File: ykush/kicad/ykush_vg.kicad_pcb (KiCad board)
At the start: 2 copper layers, 89.9 x 54.9 mm, 61 parts, among them J1 USB-C 16P, J2 USB-A port, J3 USB-A port, J4 USB-A port, J5 EXT 5V, SW1 BOOT, U1 FE1.1s, U2 USBLC6-2SC6, U3 CH552G, U4 SY6280AAC, U5 USBLC6-2SC6, U6 SY6280AAC, U7 USBLC6-2SC6, U8 SY6280AAC, U9 USBLC6-2SC6, Y1 12MHz

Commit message: YKUSH-VG: rework USB-C entry (JP1 on D-, VBUS via B.Cu spine, drop upstream ESD), move hub decoupling
Board file is still work in progress (routing run in progress).

Co-Authored-By: Claude Opus 5.5 <noreply@anthropic.com>
Claude-Session: https://claude.ai/code/session_01EEWbo5vCC8AQXSYmE1aT85
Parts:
- removed U9: USBLC6-2SC6, Package_TO_SOT_SMD:SOT-23-6
- U2: value USBLC6-2SC6 -> CH552G; footprint Package_TO_SOT_SMD:SOT-23-6 -> Package_SO:SOIC-16_3.9x9.9mm_P1.27mm
- U3: value CH552G -> SY6280AAC; footprint Package_SO:SOIC-16_3.9x9.9mm_P1.27mm -> Package_TO_SOT_SMD:SOT-23-5
- U4, U6, U8: value SY6280AAC -> USBLC6-2SC6; footprint Package_TO_SOT_SMD:SOT-23-5 -> Package_TO_SOT_SMD:SOT-23-6
- U5, U7: value USBLC6-2SC6 -> SY6280AAC; footprint Package_TO_SOT_SMD:SOT-23-6 -> Package_TO_SOT_SMD:SOT-23-5
- moved U7 32.9 mm to (181.4, 93.3), turned to 0 degrees
- moved U3 28.1 mm to (115.8, 93.3), turned to 180 degrees
- moved U5 24.5 mm to (144.4, 94.1), turned to 180 degrees
- moved U2 16.7 mm to (139.2, 77.7)
- moved C6 16.0 mm to (154.7, 88.7), turned to -90 degrees
- moved C5 13.7 mm to (156.6, 88.7), turned to -90 degrees
- moved U4 6.37 mm to (120.2, 97.9), turned to 90 degrees
- moved U8 6.37 mm to (177.0, 97.9), turned to 90 degrees
- moved U6 5.81 mm to (148.8, 97.9), turned to 90 degrees
- moved C3 5.30 mm to (148.4, 74.2)
- moved R4 4.81 mm to (158.3, 88.7), turned to -90 degrees
- moved R1 1.90 mm to (156.4, 71.7)
- moved JP1 0.73 mm to (151.9, 71.8)
- moved C4 0.50 mm to (149.5, 77.9)
- moved C7 0.36 mm to (146.7, 77.7)
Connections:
- J1 pad A6: UP_DP_A -> UP_DP
- J1 pad A7: UP_DM -> UP_DM_A
- JP1 pad 1: UP_DP_A -> UP_DM_A
- JP1 pad 2: UP_DP -> UP_DM
- U2 pad 1: UP_DP -> LED_STAT
- U2 pad 2: GND -> unconnected-(U2-P1.4-Pad2)
- U2 pad 3: UP_DM -> unconnected-(U2-P1.5-Pad3)
- U2 pad 4: UP_DM -> unconnected-(U2-P1.6-Pad4)
- U2 pad 5: VBUS_UP -> unconnected-(U2-P1.7-Pad5)
- U2 pad 6: UP_DP -> unconnected-(U2-RST-Pad6)
- U3 pad 1: LED_STAT -> VBUS_P1
- U3 pad 2: unconnected-(U3-P1.4-Pad2) -> GND
- U3 pad 3: unconnected-(U3-P1.5-Pad3) -> ISET1
- U3 pad 4: unconnected-(U3-P1.6-Pad4) -> EN1
- U3 pad 5: unconnected-(U3-P1.7-Pad5) -> +5V_PORT
- U4 pad 1: VBUS_P1 -> P1_DP
- U4 pad 3: ISET1 -> P1_DM
- U4 pad 4: EN1 -> P1_DM
- U4 pad 5: +5V_PORT -> VBUS_P1
- U5 pad 1: P1_DP -> VBUS_P2
- U5 pad 3: P1_DM -> ISET2
- U5 pad 4: P1_DM -> EN2
- U5 pad 5: VBUS_P1 -> +5V_PORT
- U6 pad 1: VBUS_P2 -> P2_DP
- U6 pad 3: ISET2 -> P2_DM
- U6 pad 4: EN2 -> P2_DM
- U6 pad 5: +5V_PORT -> VBUS_P2
- U7 pad 1: P2_DP -> VBUS_P3
- U7 pad 3: P2_DM -> ISET3
- U7 pad 4: P2_DM -> EN3
- U7 pad 5: VBUS_P2 -> +5V_PORT
- U8 pad 1: VBUS_P3 -> P3_DP
- U8 pad 3: ISET3 -> P3_DM
- U8 pad 4: EN3 -> P3_DM
- U8 pad 5: +5V_PORT -> VBUS_P3
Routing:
- net +5V_PORT: track 152.6 -> 0.00 mm
- net P2_DM: track 86.7 -> 0.00 mm, vias 2 -> 0
- net VBUS_UP: track 73.5 -> 0.00 mm, vias 1 -> 0
- net EN2: track 53.9 -> 0.00 mm, vias 4 -> 0
- net VBUS_P3: track 48.4 -> 0.00 mm, vias 2 -> 0
- net MCU_DP: track 44.3 -> 0.00 mm, vias 3 -> 0
- net LED_STAT: track 41.7 -> 0.00 mm, vias 2 -> 0
- net EN1: track 40.7 -> 0.00 mm
- net P1_DP: track 39.6 -> 0.00 mm, vias 2 -> 0
- net P3_DM: track 39.5 -> 0.00 mm, vias 4 -> 0
- net P3_DP: track 33.4 -> 0.00 mm, vias 1 -> 0
- net VBUS_P1: track 25.0 -> 0.00 mm
- net P2_DP: track 20.5 -> 0.00 mm
- net MCU_DM: track 20.4 -> 0.00 mm
- net UP_DP: track 15.4 -> 0.00 mm
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
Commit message: YKUSH-VG: rotate port ESDs so D-/D+ line up with the USB-A pins
Co-Authored-By: Claude Opus 5.5 <noreply@anthropic.com>
Claude-Session: https://claude.ai/code/session_01EEWbo5vCC8AQXSYmE1aT85
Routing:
- net +5V_PORT: track 0.00 -> 155.9 mm, vias 0 -> 6
- net EN3: track 0.00 -> 85.6 mm, vias 0 -> 2
- net EN2: track 0.00 -> 81.8 mm, vias 0 -> 3
- net ISET3: track 0.00 -> 74.9 mm, vias 0 -> 5
- net VBUS_UP: track 0.00 -> 71.2 mm, vias 0 -> 4
- net EN1: track 0.00 -> 60.8 mm
- net LED_STAT: track 0.00 -> 59.9 mm, vias 0 -> 6
- net P2_DP: track 0.00 -> 49.0 mm
- net MCU_DM: track 0.00 -> 42.1 mm, vias 0 -> 2
- net P1_DP: track 0.00 -> 39.4 mm, vias 0 -> 1
- net P3_DP: track 0.00 -> 33.3 mm
- net VBUS_P3: track 0.00 -> 33.0 mm
- net MCU_DP: track 0.00 -> 25.4 mm, vias 0 -> 1
- net VBUS_P1: track 0.00 -> 25.0 mm
- net +3V3: track 0.00 -> 23.3 mm
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
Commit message: YKUSH-VG: keep KiCad net names, GND stub pass, DRC helper fixes, silk checks off (no silkscreen on Viagrid)
Board file still in progress.

Co-Authored-By: Claude Opus 5.5 <noreply@anthropic.com>
Claude-Session: https://claude.ai/code/session_01EEWbo5vCC8AQXSYmE1aT85
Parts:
- turned U4 to -90 degrees
- turned U6 to -90 degrees
- turned U8 to -90 degrees
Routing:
- net P1_DM: track 0.00 -> 49.3 mm, vias 0 -> 5
- net P3_DM: track 0.00 -> 35.4 mm
- net EN2: track 81.8 -> 57.9 mm, vias 3 -> 2
- net P2_DM: track 0.00 -> 16.3 mm
- net P2_DP: track 49.0 -> 43.0 mm, vias 0 -> 2
- net P1_DP: track 39.4 -> 43.6 mm
- net VBUS_P3: track 33.0 -> 29.4 mm
- net VBUS_P2: track 20.2 -> 23.3 mm
- net +5V_PORT: track 155.9 -> 158.0 mm
- net VBUS_P1: track 25.0 -> 27.0 mm
- net MCU_DM: track 42.1 -> 43.9 mm, vias 2 -> 6
- net LED_STAT: track 59.9 -> 58.3 mm, vias 6 -> 4
- net P3_DP: track 33.3 -> 34.6 mm
- net EN3: track 85.6 -> 86.5 mm
- net EN1: track 60.8 -> 60.2 mm, vias 0 -> 1
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
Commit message: WIP board snapshot (routing run in progress)
Co-Authored-By: Claude Opus 5.5 <noreply@anthropic.com>
Claude-Session: https://claude.ai/code/session_01EEWbo5vCC8AQXSYmE1aT85
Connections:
- net +1V8 renamed /+1V8
- net +3V3 renamed /+3V3
- net +5V_PORT renamed /+5V_PORT
- net BOOT_R renamed /BOOT_R
- net CC1 renamed /CC1
- net CC2 renamed /CC2
- net EN1 renamed /EN1
- net EN2 renamed /EN2
- net EN3 renamed /EN3
- net EXT_5V renamed /EXT_5V
- net EXT_5V_IN renamed /EXT_5V_IN
- net GND renamed /GND
- net ISET1 renamed /ISET1
- net ISET2 renamed /ISET2
- net ISET3 renamed /ISET3
- net LED_P1 renamed /LED_P1
- net LED_P2 renamed /LED_P2
- net LED_P3 renamed /LED_P3
- net LED_PWR renamed /LED_PWR
- net LED_STAT renamed /LED_STAT
- net LED_STAT_A renamed /LED_STAT_A
- net MCU_DM renamed /MCU_DM
- net MCU_DP renamed /MCU_DP
- net P1_DM renamed /P1_DM
- net P1_DP renamed /P1_DP
- net P2_DM renamed /P2_DM
- net P2_DP renamed /P2_DP
- net P3_DM renamed /P3_DM
- net P3_DP renamed /P3_DP
- net REXT renamed /REXT
- net UP_DM renamed /UP_DM
- net UP_DM_A renamed /UP_DM_A
- net UP_DP renamed /UP_DP
- net V33_MCU renamed /V33_MCU
- net VBUSM renamed /VBUSM
- net VBUS_P1 renamed /VBUS_P1
- net VBUS_P2 renamed /VBUS_P2
- net VBUS_P3 renamed /VBUS_P3
- net VBUS_UP renamed /VBUS_UP
- net XIN renamed /XIN
- net XOUT renamed /XOUT
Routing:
- net /GND: track 0.00 -> 17.3 mm

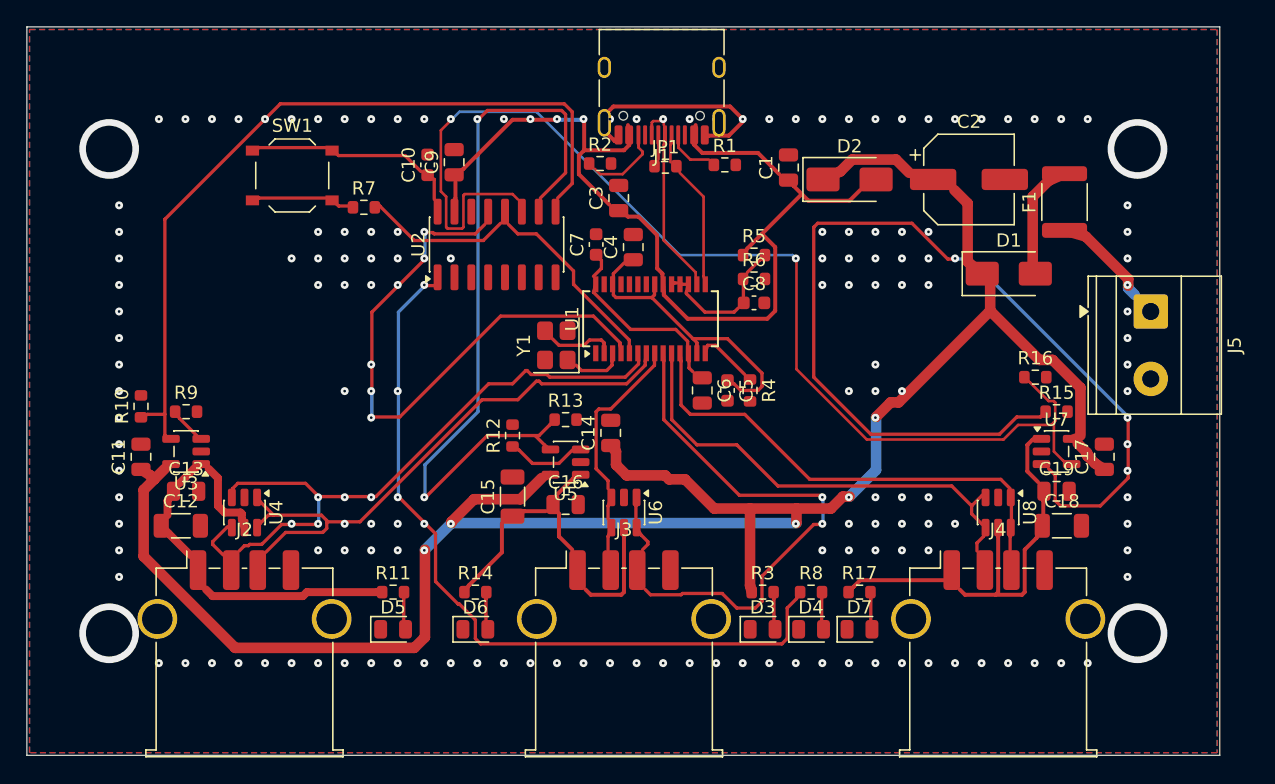
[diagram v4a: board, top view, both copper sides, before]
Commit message: WIP board snapshot (reroute in progress)
Co-Authored-By: Claude Opus 5.5 <noreply@anthropic.com>
Claude-Session: https://claude.ai/code/session_01EEWbo5vCC8AQXSYmE1aT85
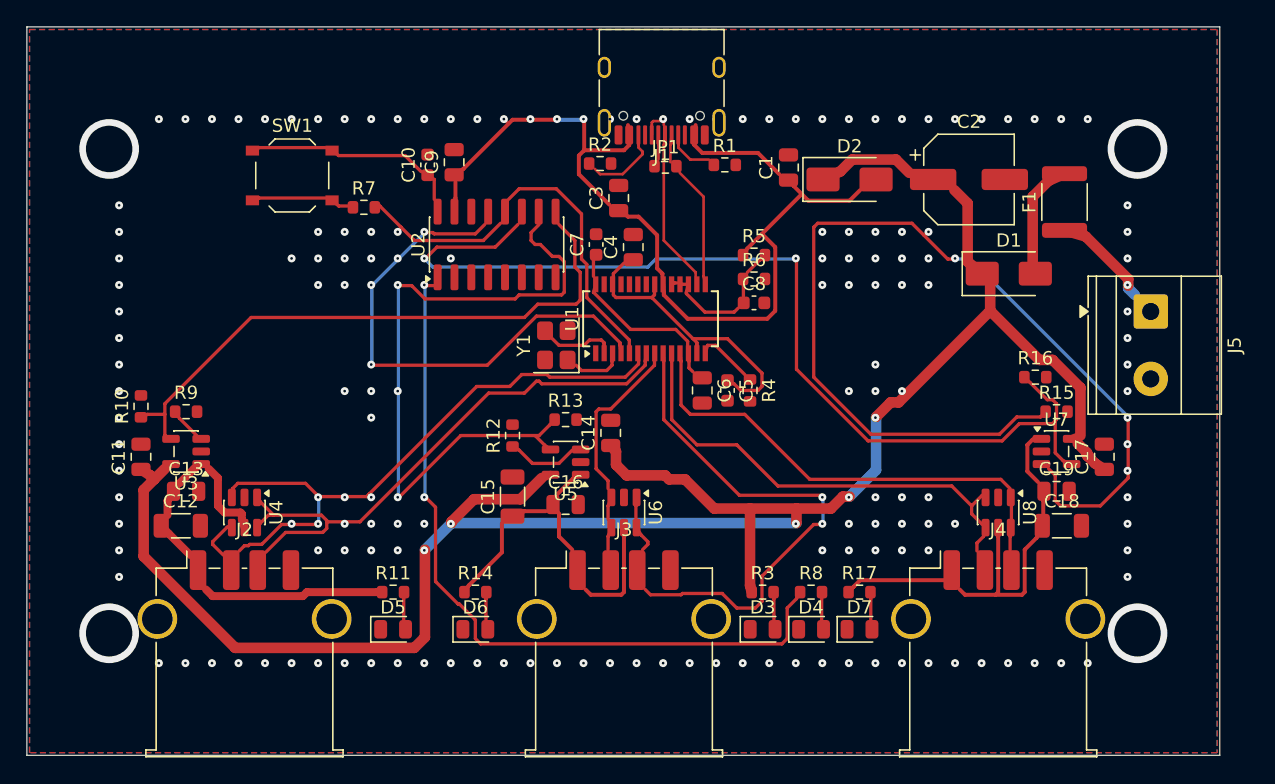
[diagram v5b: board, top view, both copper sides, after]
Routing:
- net /GND: track 17.3 -> 0.00 mm, vias 143 -> 147
- net /EN1: track 60.2 -> 45.7 mm, vias 1 -> 0
- net /EN3: track 86.5 -> 75.8 mm
- net /EN2: track 57.9 -> 51.8 mm, vias 2 -> 3
- net /MCU_DM: track 43.9 -> 38.5 mm, vias 6 -> 4
- net /MCU_DP: track 25.4 -> 30.1 mm
- net /LED_STAT: track 58.3 -> 56.6 mm, vias 4 -> 2
- net /ISET3: track 74.9 -> 75.5 mm
- net /VBUS_UP: track 71.2 -> 71.7 mm
- net /+5V_PORT: track 158.0 -> 158.5 mm

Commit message: WIP board snapshot
Co-Authored-By: Claude Opus 5.5 <noreply@anthropic.com>
Claude-Session: https://claude.ai/code/session_01EEWbo5vCC8AQXSYmE1aT85
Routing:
- net /+3V3: track 23.3 -> 79.3 mm, vias 0 -> 4
- net /EN2: track 51.8 -> 0.00 mm, vias 3 -> 0
- net /GND: track 0.00 -> 33.1 mm, vias 147 -> 156
- net /MCU_DP: track 30.1 -> 0.00 mm, vias 1 -> 0
- net /ISET3: track 75.5 -> 48.2 mm, vias 5 -> 3
- net /EN3: track 75.8 -> 96.0 mm
- net /P2_DP: track 43.0 -> 57.4 mm, vias 2 -> 3
- net /MCU_DM: track 38.5 -> 24.4 mm, vias 4 -> 0
- net /P2_DM: track 16.3 -> 27.9 mm
- net /P1_DM: track 49.6 -> 39.3 mm, vias 5 -> 0
- net /P1_DP: track 43.7 -> 38.9 mm, vias 1 -> 0
- net /EN1: track 45.7 -> 41.1 mm, vias 0 -> 1
- net /ISET2: track 5.40 -> 9.01 mm
- net /LED_STAT: track 56.6 -> 59.4 mm, vias 2 -> 3
- net /P3_DP: track 34.6 -> 35.8 mm
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
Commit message: WIP board snapshot
Co-Authored-By: Claude Opus 5.5 <noreply@anthropic.com>
Claude-Session: https://claude.ai/code/session_01EEWbo5vCC8AQXSYmE1aT85
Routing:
- net /EN3: track 96.0 -> 0.00 mm, vias 2 -> 0
- net /+3V3: track 79.3 -> 20.0 mm, vias 4 -> 0
- net /ISET3: track 48.2 -> 7.52 mm, vias 3 -> 0
- net /MCU_DP: track 0.00 -> 30.1 mm, vias 0 -> 1
- net /GND: track 33.1 -> 58.7 mm, vias 156 -> 161
- net /LED_STAT: track 59.4 -> 41.7 mm, vias 3 -> 2
- net /P2_DP: track 57.4 -> 45.8 mm, vias 3 -> 0
- net /P2_DM: track 27.9 -> 17.2 mm
- net /+5V_PORT: track 158.9 -> 151.0 mm
- net /MCU_DM: track 24.4 -> 32.2 mm, vias 0 -> 3
- net /P1_DP: track 38.9 -> 43.4 mm, vias 0 -> 2
- net /CC2: track 5.97 -> 9.58 mm, vias 0 -> 2
- net /VBUS_UP: track 71.7 -> 73.8 mm, vias 4 -> 1
- net /VBUS_P3: track 29.4 -> 31.3 mm
- net /P1_DM: track 39.3 -> 40.4 mm, vias 0 -> 1
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
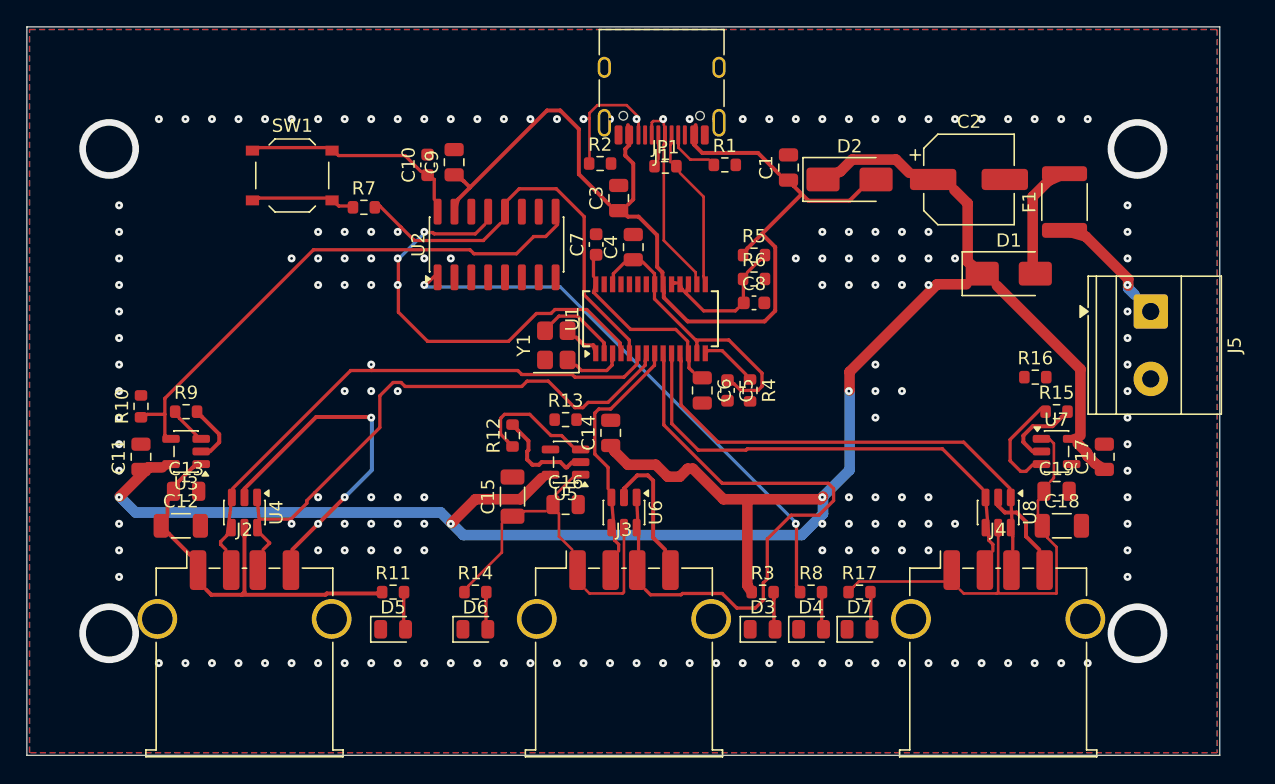
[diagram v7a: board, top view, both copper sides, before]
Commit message: Route GND as a net (pads to nearest Viagrid via); finish pass (retry unrouted nets, sync pin changes); EN1 moved to CH552 P1.4; geometric pour-island detection
Co-Authored-By: Claude Opus 5.5 <noreply@anthropic.com>
Claude-Session: https://claude.ai/code/session_01EEWbo5vCC8AQXSYmE1aT85
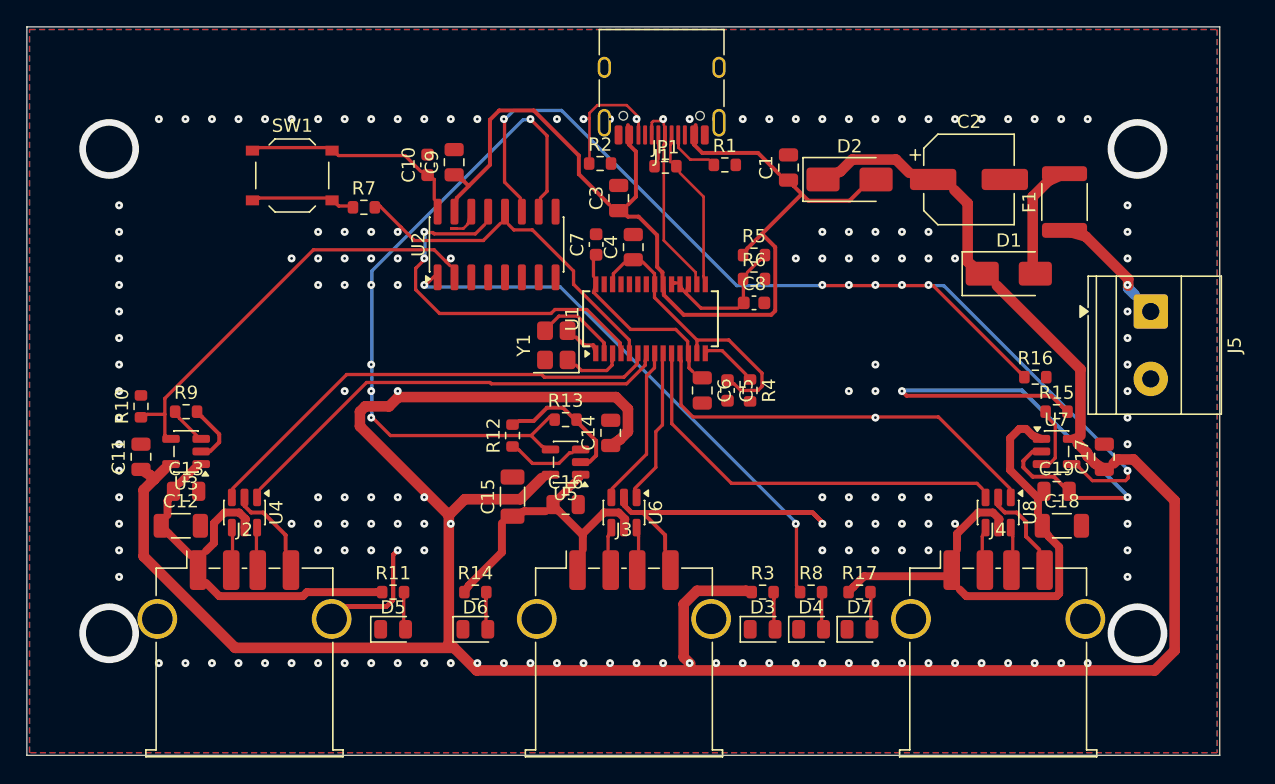
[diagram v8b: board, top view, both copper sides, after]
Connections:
- U2 pad 2: unconnected-(U2-P1.4-Pad2) -> /EN1
- U2 pad 9: /EN1 -> unconnected-(U2-P1.1-Pad9)
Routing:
- net /GND: track 58.7 -> 183.4 mm, vias 161 -> 133
- net /EN3: track 0.00 -> 80.7 mm, vias 0 -> 7
- net /+5V_PORT: track 151.0 -> 219.6 mm, vias 6 -> 27
- net /EN2: track 0.00 -> 51.4 mm, vias 0 -> 5
- net /P2_DP: track 45.8 -> 12.8 mm
- net /EN1: track 40.4 -> 32.2 mm, vias 0 -> 1
- net /P1_DP: track 43.4 -> 35.5 mm, vias 2 -> 0
- net /VBUS_P3: track 31.3 -> 37.5 mm, vias 0 -> 1
- net /MCU_DM: track 32.2 -> 27.5 mm, vias 3 -> 2
- net /MCU_DP: track 30.1 -> 25.8 mm
- net /P2_DM: track 17.2 -> 13.2 mm
- net /ISET2: track 9.01 -> 5.32 mm
- net /P1_DM: track 40.4 -> 37.0 mm, vias 1 -> 0
- net /ISET3: track 7.52 -> 4.32 mm
- net /VBUS_P2: track 23.3 -> 20.4 mm
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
